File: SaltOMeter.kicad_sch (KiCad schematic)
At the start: 20 parts, among them J1 USB_C_Receptacle_USB2.0_16P, Q1 AO3401A, SW1 SW_SPST, U1 ESP32-S3-WROOM-1, U2 TP4056-42-ESOP8, U3 AP2112K-3.3

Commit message: rgwgrfs
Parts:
- added J2: Motor1, Connector_JST:JST_XH_B2B-XH-A_1x02_P2.50mm_Vertical, symbol Connector:Conn_01x02_Socket
- added J3: Motor2, Connector_JST:JST_XH_B2B-XH-A_1x02_P2.50mm_Vertical, symbol Connector:Conn_01x02_Socket
- added R7: 10k, symbol Device:R
- added U4: DRV8833PW, Package_SO:TSSOP-16_4.4x5mm_P0.65mm, symbol Driver_Motor:DRV8833PW
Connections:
- net GND: now also U4.13 (GND)
- net VMAIN: now also R7.1, U4.12 (VM)
- net MOTOR_IN1: now reaches U1.4 (IO4)
- net MOTOR_IN1: now also U4.16 (AIN1)
- net MOTOR_IN2: now reaches U1.5 (IO5)
- net MOTOR_IN2: now also U4.15 (AIN2)
- net MOTOR_IN3: now reaches U1.6 (IO6)
- net MOTOR_IN3: now also U4.9 (BIN1)
- net MOTOR_IN4: now reaches U1.7 (IO7)
- net MOTOR_IN4: now also U4.10 (BIN2)
- net I2C_SDA: now reaches U1.8 (IO15)
- net I2C_SDL: now reaches U1.9 (IO16)
- new net: R7.2, U4.1 (~{SLEEP})
- new net: J3.1 (Pin_1), U4.7 (BOUT1)
- new net: J3.2 (Pin_2), U4.5 (BOUT2)
- new net: J2.1 (Pin_1), U4.2 (AOUT1)
- new net: J2.2 (Pin_2), U4.4 (AOUT2)

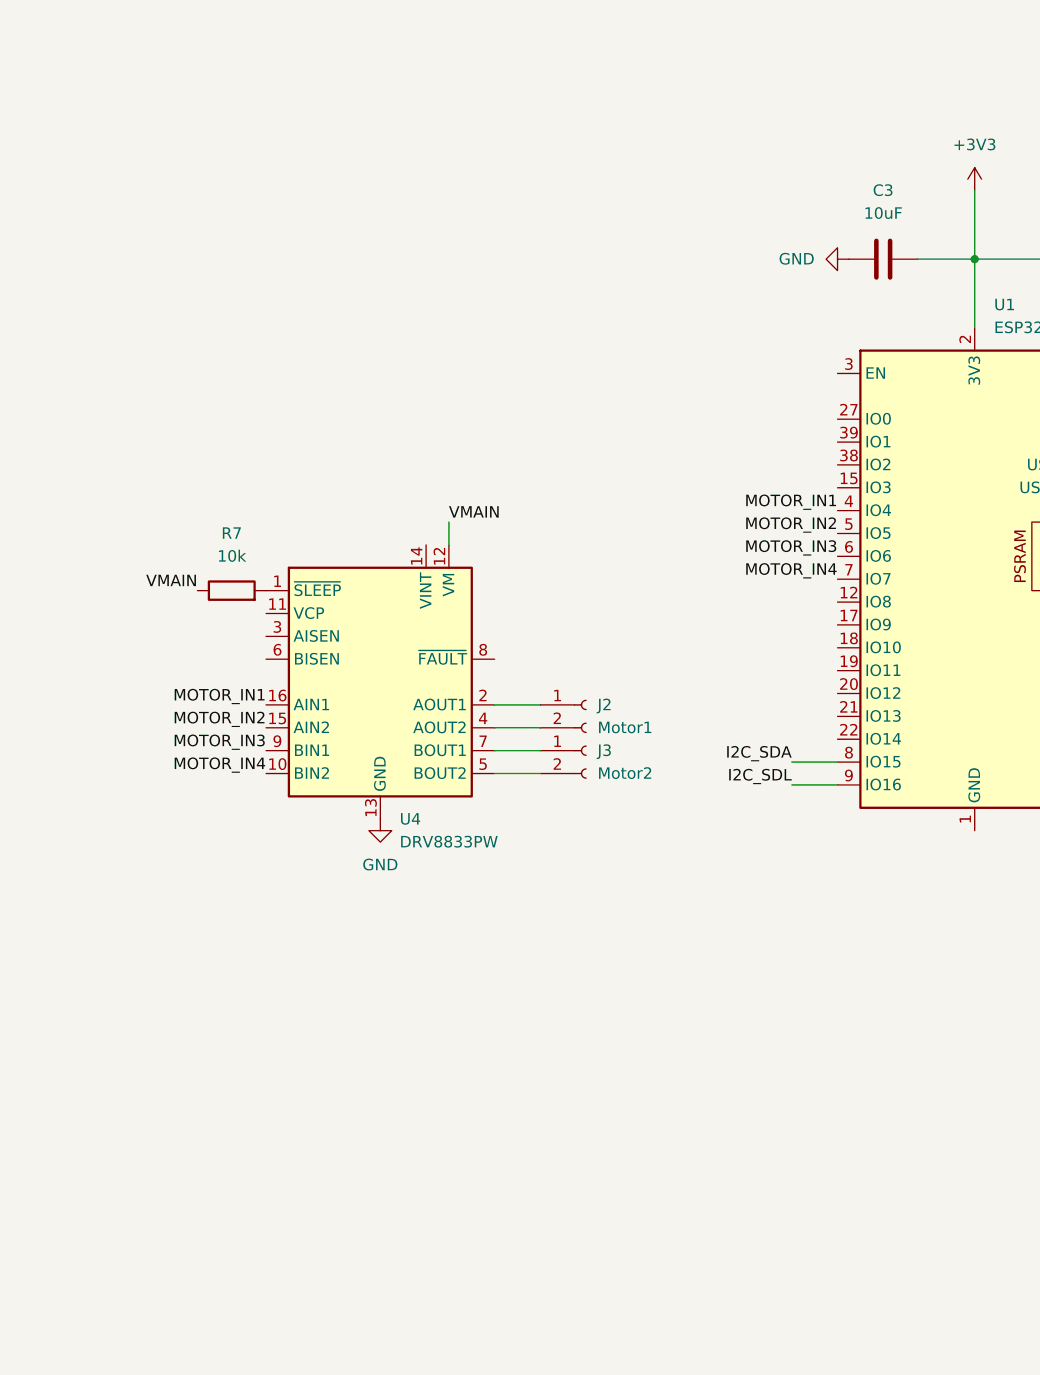
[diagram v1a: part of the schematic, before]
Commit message: add speaker and afefw
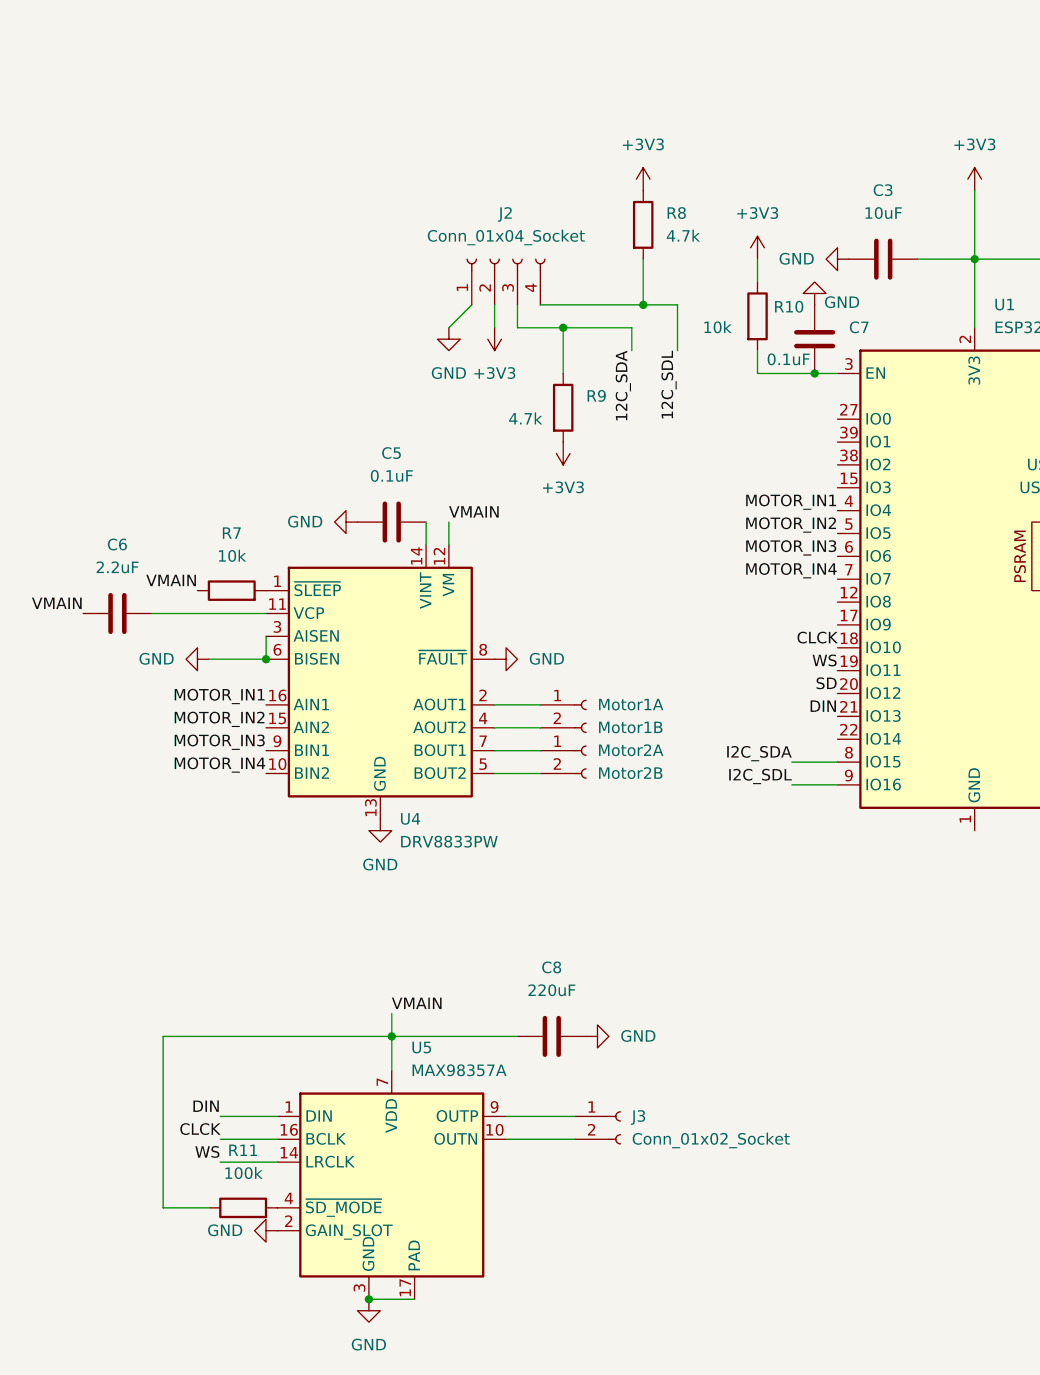
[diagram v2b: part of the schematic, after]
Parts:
- added C5, C7: 0.1uF, symbol Device:C
- added C6: 2.2uF, symbol Device:C
- added C8: 220uF, symbol Device:C
- added J2: Conn_01x04_Socket, Connector_JST:JST_XH_B4B-XH-A_1x04_P2.50mm_Vertical, symbol Connector:Conn_01x04_Socket
- added J3: Conn_01x02_Socket, Connector_JST:JST_XH_B2B-XH-AM_1x02_P2.50mm_Vertical, symbol Connector:Conn_01x02_Socket
- added R10: 10k, symbol Device:R
- added R11: 100k, symbol Device:R
- added R8, R9: 4.7k, symbol Device:R
- added U5: MAX98357A, Package_DFN_QFN:TQFN-16-1EP_3x3mm_P0.5mm_EP1.23x1.23mm, symbol Audio:MAX98357A
- Motor1A: renamed from J2; value Motor1 -> Motor1B
- Motor2A: renamed from J3; value Motor2 -> Motor2B
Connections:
- net +3V3: now also J2.2 (Pin_2), R10.1, R8.1, R9.2
- net GND: now also U4.3 (AISEN), U4.6 (BISEN), U4.8 (~{FAULT}), C5.1, C7.2, C8.2, J2.1 (Pin_1), U5.11 (GND), U5.15 (GND), U5.17 (PAD), U5.2 (GAIN_SLOT), U5.3 (GND)
- net VMAIN: now also C6.1, C8.1, R11.1, U5.7 (VDD), U5.8 (VDD)
- net CLCK: now reaches U1.18 (IO10)
- net CLCK: now also U5.16 (BCLK)
- net WS: now reaches U1.19 (IO11)
- net WS: now also U5.14 (LRCLK)
- net SD: now reaches U1.20 (IO12)
- net DIN: now reaches U1.21 (IO13)
- net DIN: now also U5.1 (DIN)
- net at U1.3 (EN): now also C7.1, R10.2
- net at U4.11 (VCP): now also C6.2
- net at U4.14 (VINT): now also C5.2
- new net: R11.2, U5.4 (~{SD_MODE})
- new net: J3.2 (Pin_2), U5.10 (OUTN)
- new net: J3.1 (Pin_1), U5.9 (OUTP)
- new net 12C_SDA: J2.3 (Pin_3), R9.1
- new net 12C_SDL: J2.4 (Pin_4), R8.2

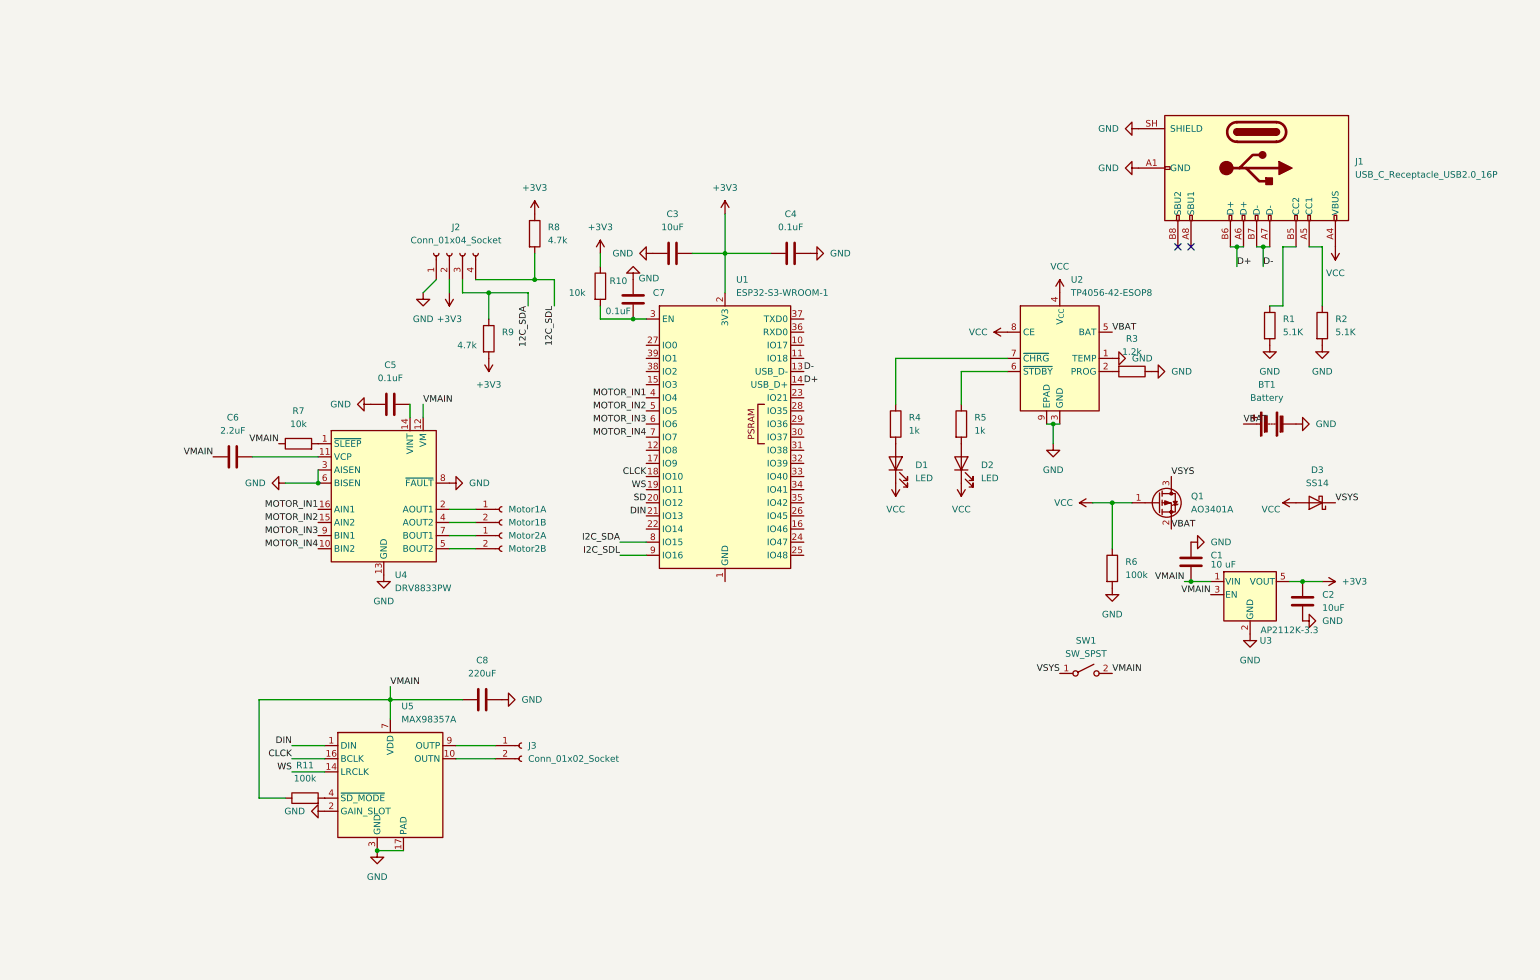
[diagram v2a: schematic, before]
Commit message: Finish schematic and start work on PCB
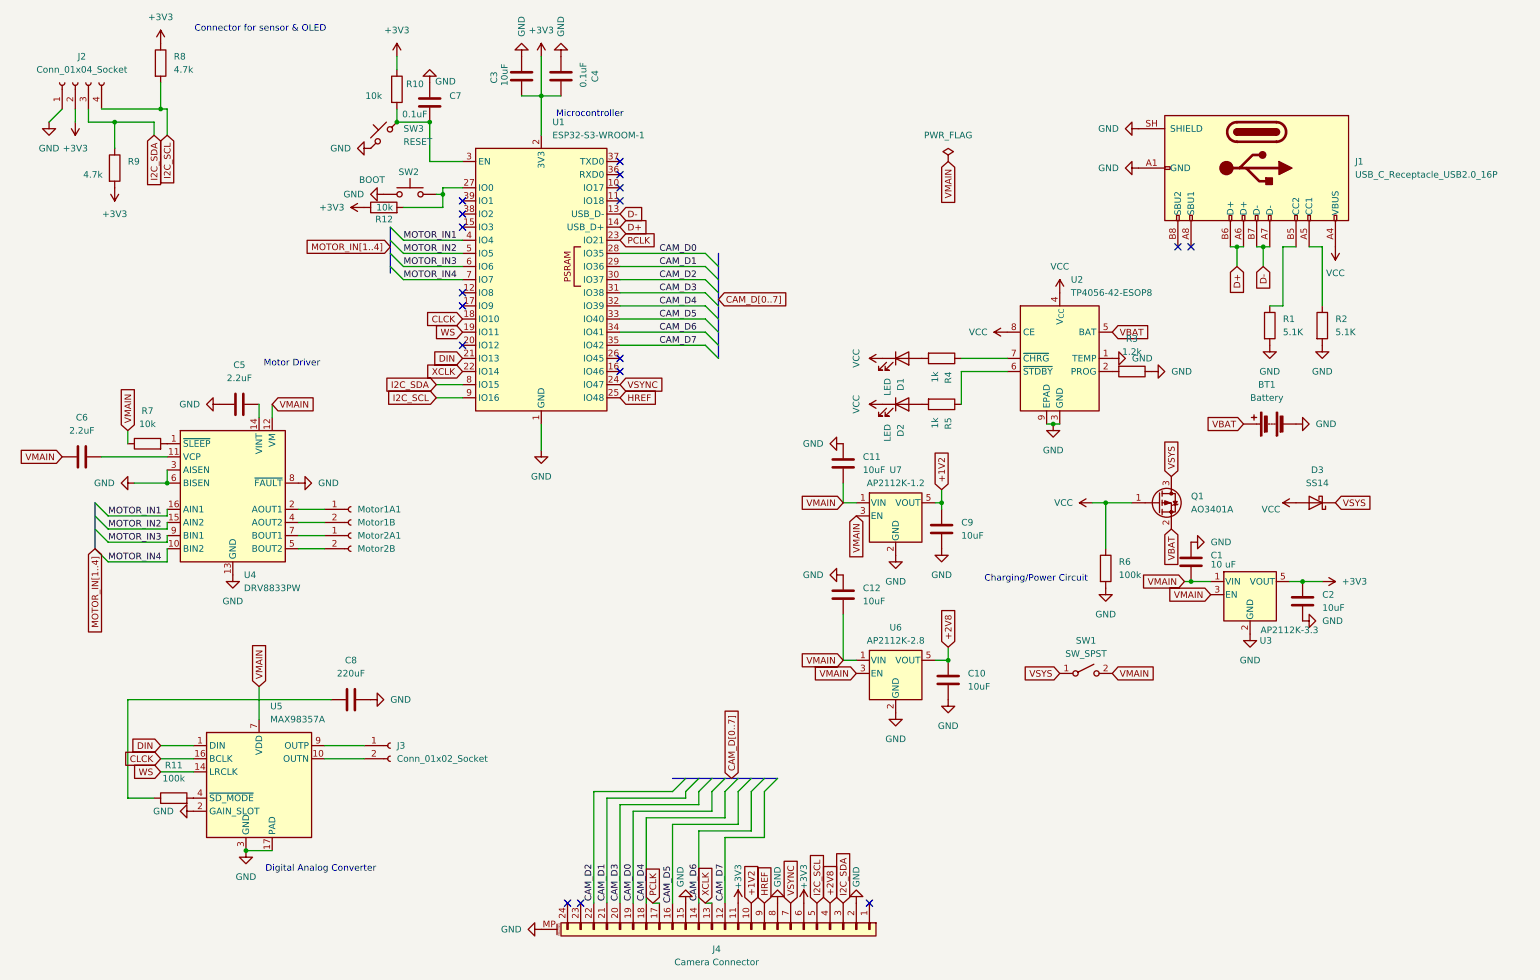
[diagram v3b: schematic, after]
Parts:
- added C10, C11, C12, C9: 10uF, Capacitor_SMD:C_0805_2012Metric_Pad1.18x1.45mm_HandSolder, symbol Device:C
- added J4: Camera Connector, Connector_FFC-FPC:Molex_200528-0240_1x24-1MP_P1.00mm_Horizontal, symbol Connector_Generic_MountingPin:Conn_01x24_MountingPin
- added R12: 10k, Resistor_SMD:R_0805_2012Metric_Pad1.20x1.40mm_HandSolder, symbol Device:R
- added SW2: BOOT, Button_Switch_SMD:SW_SPST_B3S-1000, symbol Switch:SW_Push
- added SW3: RESET, Button_Switch_SMD:SW_SPST_B3S-1000, symbol Switch:SW_Push_45deg
- added U6: AP2112K-2.8, Package_TO_SOT_SMD:SOT-23-5, symbol Regulator_Linear:AP2112K-2.6
- added U7: AP2112K-1.2, Package_TO_SOT_SMD:SOT-23-5, symbol Regulator_Linear:AP2112K-1.2
- BT1: footprint (none) -> Connector_JST:JST_PH_S2B-PH-K_1x02_P2.00mm_Horizontal
- C1, C2, C3, C4, C6, C7, C8: footprint (none) -> Capacitor_SMD:C_0805_2012Metric_Pad1.18x1.45mm_HandSolder
- C5: value 0.1uF -> 2.2uF; footprint (none) -> Capacitor_SMD:C_0805_2012Metric_Pad1.18x1.45mm_HandSolder
- D1, D2: footprint (none) -> LED_SMD:LED_0805_2012Metric_Pad1.15x1.40mm_HandSolder
- R1, R10, R11, R2, R3, R4, R5, R6, R7, R8, R9: footprint (none) -> Resistor_SMD:R_0805_2012Metric_Pad1.20x1.40mm_HandSolder
- SW1: footprint (none) -> Button_Switch_THT:SW_Slide_SPDT_Straight_CK_OS102011MS2Q
- renumbered Motor1A to Motor1A1, Motor2A to Motor2A1
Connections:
- net 12C_SDA is gone; now on net I2C_SDA: J2.3 (Pin_3), R9.1
- net I2C_SDL is gone; now on net I2C_SCL: U1.9 (IO16)
- net +3V3: now also J4.11 (Pin_11), J4.6 (Pin_6), R12.1
- net GND: now also U1.1 (GND), U1.40 (GND), U1.41 (GND), C10.2, C11.2, C12.1, C9.2, J4.15 (Pin_15), J4.2 (Pin_2), J4.8 (Pin_8), J4.MP (MountPin), SW2.1, SW3.1, U6.2 (GND), U7.2 (GND)
- net I2C_SDA: now also J4.3 (Pin_3)
- net VMAIN: now also C11.1, C12.2, U6.1 (VIN), U6.3 (EN), U7.1 (VIN), U7.3 (EN); no longer C8.1, R11.1
- net at C7.1, R10.2, U1.3 (EN): now also SW3.2
- net XCLK: now reaches U1.22 (IO14)
- net XCLK: now also J4.13 (Pin_13)
- net PCLK: now reaches U1.23 (IO21)
- net PCLK: now also J4.17 (Pin_17)
- net VSYNC: now reaches U1.24 (IO47)
- net VSYNC: now also J4.7 (Pin_7)
- net HREF: now reaches U1.25 (IO48)
- net HREF: now also J4.9 (Pin_9)
- net at U1.27 (IO0): now also R12.2, SW2.2
- net CAM_D0: now reaches U1.28 (IO35)
- net CAM_D0: now also J4.19 (Pin_19)
- net CAM_D1: now reaches U1.29 (IO36)
- net CAM_D1: now also J4.21 (Pin_21)
- net at U1.30 (IO37): no longer names the net of U1.30 (IO37)
- net at U1.30 (IO37): now also J4.22 (Pin_22)
- net CAM_D3: now reaches U1.31 (IO38)
- net CAM_D3: now also J4.20 (Pin_20)
- net CAM_D4: now reaches U1.32 (IO39)
- net CAM_D4: now also J4.18 (Pin_18)
- net CAM_D5: now reaches U1.33 (IO40)
- net CAM_D5: now also J4.16 (Pin_16)
- net CAM_D6: now reaches U1.34 (IO41)
- net CAM_D6: now also J4.14 (Pin_14)
- net CAM_D7: now reaches U1.35 (IO42)
- net CAM_D7: now also J4.12 (Pin_12)
- net 12C_SDL renamed I2C_SCL
- net I2C_SCL: now also J4.5 (Pin_5)
- net SD: no longer names the net of U1.20 (IO12)
- new net: C8.1, R11.1
- new net +1V2: C9.1, J4.10 (Pin_10), U7.5 (VOUT)
- new net +2V8: C10.1, J4.4 (Pin_4), U6.5 (VOUT)
- no-connect marks 2 -> 17
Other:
- note added: "Charging/Power Circuit"
- note added: "Connector for sensor & OLED"
- note added: "Digital Analog Converter"
- note added: "Microcontroller"
- note added: "Motor Driver"
- moved on the sheet: C3, C4, C5, C6, C7, C8, D1, D2, J2, J3, Motor1A1, Motor2A1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

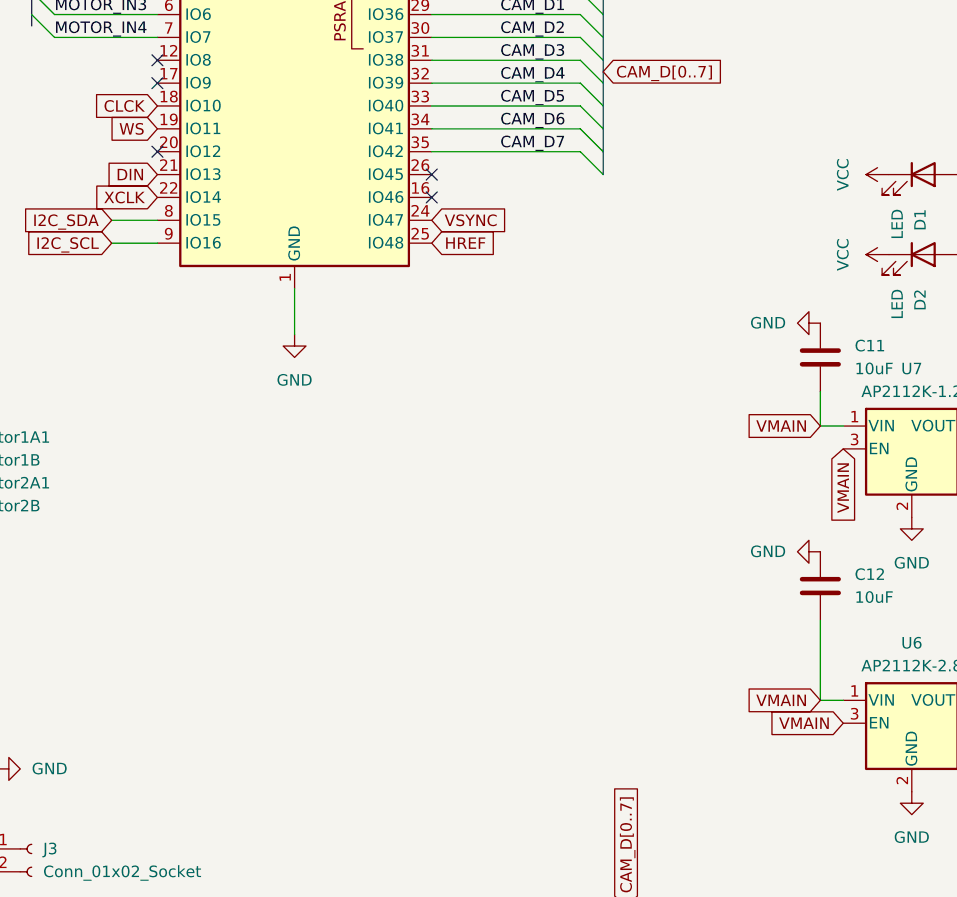
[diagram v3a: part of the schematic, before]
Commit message: add fan
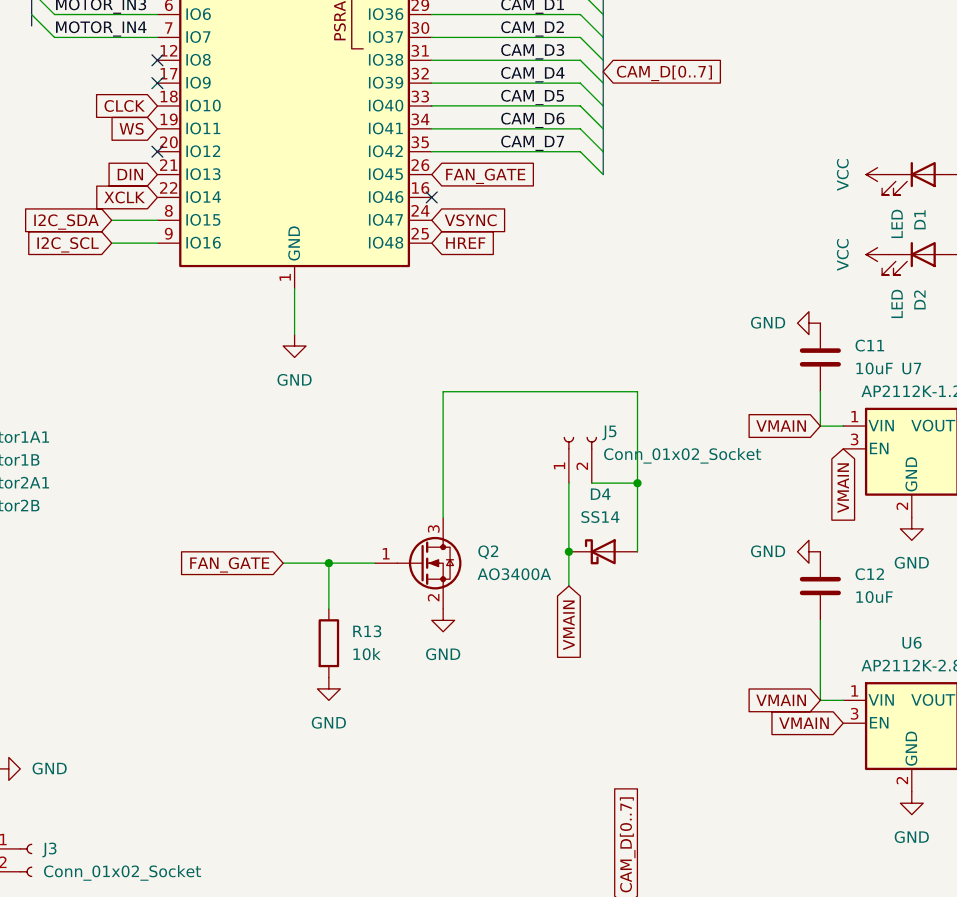
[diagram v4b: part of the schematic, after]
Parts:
- added D4: SS14, Diode_SMD:D_SMA, symbol Diode:SS14
- added J5: Conn_01x02_Socket, Connector_JST:JST_PH_B2B-PH-K_1x02_P2.00mm_Vertical, symbol Connector:Conn_01x02_Socket
- added Q2: AO3400A, Package_TO_SOT_SMD:SOT-23, symbol Transistor_FET:AO3400A
- added R13: 10k, symbol Device:R
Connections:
- net GND: now also Q2.2 (S), R13.2
- net VMAIN: now also D4.1 (K), J5.1 (Pin_1)
- net FAN_GATE: now reaches U1.26 (IO45)
- net FAN_GATE: now also Q2.1 (G), R13.1
- new net: D4.2 (A), J5.2 (Pin_2), Q2.3 (D)
- no-connect marks 17 -> 16
